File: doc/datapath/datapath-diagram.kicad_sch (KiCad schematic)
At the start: 24 parts, among them U17 ip, U19 insn, U27 stack[0], U28 stack[1], U29 ……, U32 cd_timer, U4 cstack[0], U5 cstack[1], U6 ……

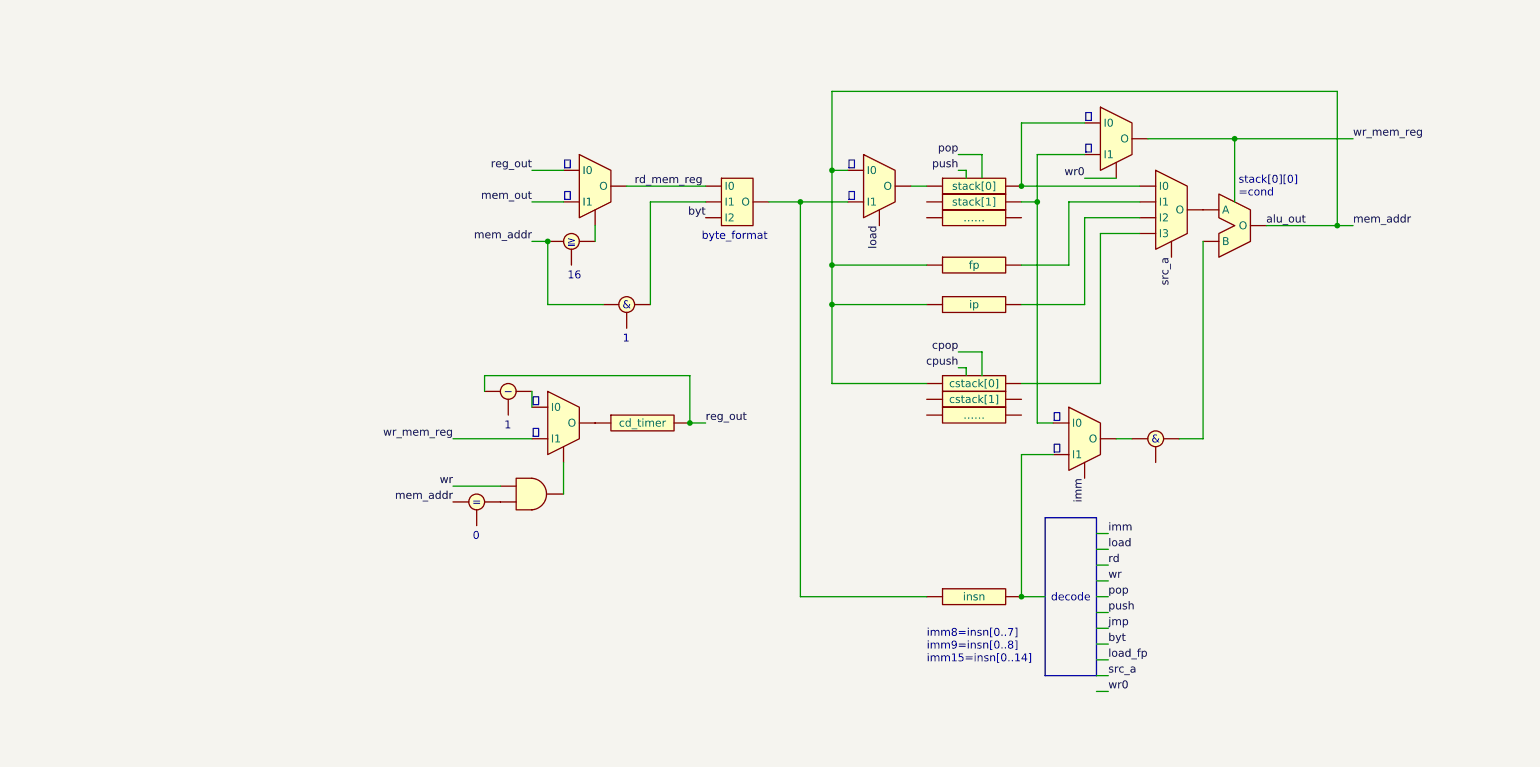
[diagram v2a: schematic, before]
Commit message: データパス図の信号名を現行の名前に合わせる
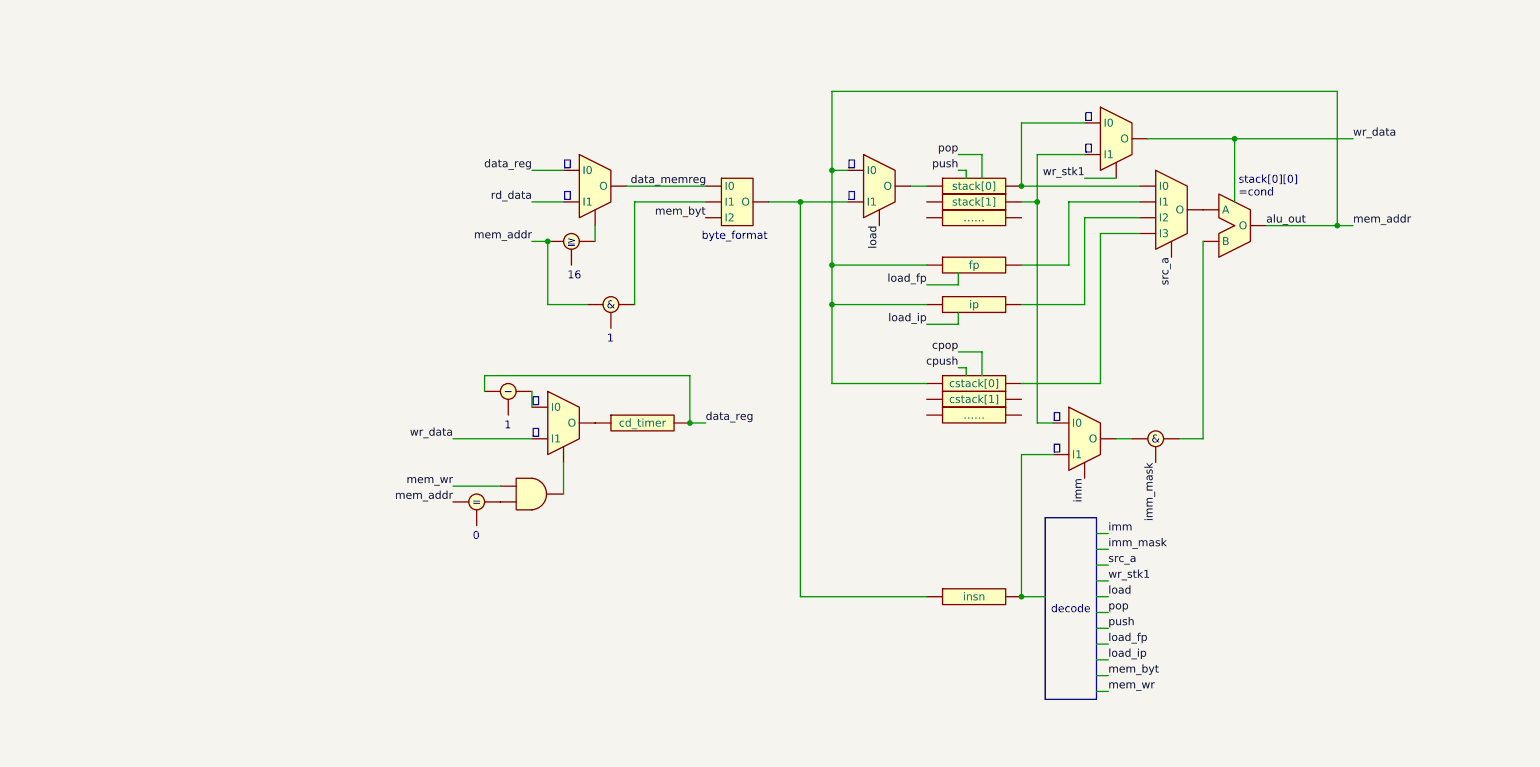
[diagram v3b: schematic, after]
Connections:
- net byt is gone; now on net mem_byt: U34. (O)
- net mem_out is gone; now on net rd_data: U31. (O)
- net wr is gone; now on net mem_wr: U39.
- net at U28.: now also U15. (O), U3. (O)
- net rd_data: now reaches U31. (O)
- net rd_data: no longer U1.
- net at U27.: now also U3. (O), U40. (O); no longer U18. (O)
- net data_reg: now reaches U32.
- net data_reg: now also U31. (O), U37.; no longer U36. (O)
- net mem_byt: now reaches U34. (O)
- net mem_byt: no longer U33.
- net wr_data: now reaches U36. (O)
- net wr_data: now also U3. (O); no longer U37.
- net imm_mask: now reaches U2.
- net mem_wr: now reaches U39.
- net mem_wr: no longer U36. (O)
- removed net rd_mem_reg: U31. (O), U34. (O)
- removed net reg_out: U31. (O), U32., U37.
- net wr0 renamed wr_stk1
- removed net wr_mem_reg: U3. (O), U36. (O)
- new net: U1., U31. (O)
- new net: U18. (O), U19., U34. (O)
- new net: U18. (O), U27.
- new net: U32., U36. (O)
- new net: U33., U34. (O)
- new net: U., U40. (O)
- new net: U17., U40. (O)
- new net: U4., U40. (O)
- new net: U12. (O), U40. (O)
- new net: U36. (O), U37.
- new net: U12. (O), U2.
- new net: U15. (O), U2.
- new net: U36. (O), U39.
- new net: U38., U39.
- new net data_memreg: U31. (O), U34. (O)
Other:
- note removed: "imm8=insn[0..7] imm9=insn[0..8] imm15=insn[0..14]"
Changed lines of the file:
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@@
     (stroke (width 0) (type default))
   )
-  (wire (pts (xy 114.3 69.85) (xy 114.3 53.34))
+  (wire (pts (xy 163.83 64.77) (xy 163.83 66.675))
+    (stroke (width 0) (type default))
+  )
+  (wire (pts (xy 111.76 69.85) (xy 111.76 53.34))
     (stroke (width 0) (type default))
   )
@@
     (stroke (width 0) (type default))
   )
-  (wire (pts (xy 97.79 69.85) (xy 106.68 69.85))
+  (wire (pts (xy 97.79 69.85) (xy 104.14 69.85))
     (stroke (width 0) (type default))
   )
@@
     (stroke (width 0) (type default))
   )
+  (wire (pts (xy 158.75 73.025) (xy 163.83 73.025))
+    (stroke (width 0) (type default))
+  )
   (wire (pts (xy 184.15 49.53) (xy 189.23 49.53))
     (stroke (width 0) (type default))
@@
     (stroke (width 0) (type default))
   )
+  (wire (pts (xy 110.49 50.8) (xy 123.19 50.8))
+    (stroke (width 0) (type default))
+  )
   (wire (pts (xy 97.79 59.69) (xy 97.79 69.85))
     (stroke (width 0) (type default))
@@
     (stroke (width 0) (type default))
   )
-  (wire (pts (xy 110.49 50.8) (xy 123.19 50.8))
+  (wire (pts (xy 163.83 71.12) (xy 163.83 73.025))
     (stroke (width 0) (type default))
   )
@@
     (stroke (width 0) (type default))
   )
+  (wire (pts (xy 158.75 66.675) (xy 163.83 66.675))
+    (stroke (width 0) (type default))
+  )
   (wire (pts (xy 208.28 43.18) (xy 208.28 53.34))
     (stroke (width 0) (type default))
@@
     (stroke (width 0) (type default))
   )
-  (wire (pts (xy 114.3 53.34) (xy 123.19 53.34))
+  (wire (pts (xy 111.76 53.34) (xy 123.19 53.34))
     (stroke (width 0) (type default))
   )
@@
   )
   (text_box "decode"
-    (at 177.8 104.14 0) (size 8.255 25.4)
+    (at 177.8 104.14 0) (size 8.255 29.21)
     (stroke (width 0) (type default))
     (fill (type color) (color 255 255 194 1))
@@
   )
   (text_box "&"
-    (at 109.22 68.58 0) (size 2.54 2.54)
+    (at 106.68 68.58 0) (size 2.54 2.54)
     (stroke (width -0.0001) (type default))
     (fill (type none))
@@
     (effects (font (size 1.27 1.27)) (justify left bottom))
   )
-  (text "imm8=insn[0..7]\nimm9=insn[0..8]\nimm15=insn[0..14]" (at 158.75 127.635 0)
-    (effects (font (size 1.27 1.27)) (justify left bottom))
-  )
   (text "偽" (at 146.05 48.26 0)
     (effects (font (size 1.27 1.27)) (justify left bottom))
@@
     (effects (font (size 1.27 1.27)) (justify left bottom))
   )
-  (text "1" (at 109.855 76.2 0)
+  (text "1" (at 107.315 76.2 0)
     (effects (font (size 1.27 1.27)) (justify left bottom))
   )
@@
     (effects (font (size 1.27 1.27)) (justify left bottom))
   )
-  (label "src_a" (at 187.96 129.54 0) (fields_autoplaced)
-    (effects (font (size 1.27 1.27)) (justify left bottom))
-  )
-  (label "mem_out" (at 95.25 53.34 180) (fields_autoplaced)
+  (label "src_a" (at 187.96 111.76 0) (fields_autoplaced)
+    (effects (font (size 1.27 1.27)) (justify left bottom))
+  )
+  (label "rd_data" (at 95.25 53.34 180) (fields_autoplaced)
     (effects (font (size 1.27 1.27)) (justify right bottom))
   )
@@
     (effects (font (size 1.27 1.27)) (justify right bottom))
   )
-  (label "wr_mem_reg" (at 227.33 43.18 0) (fields_autoplaced)
+  (label "imm_mask" (at 195.58 95.25 270) (fields_autoplaced)
+    (effects (font (size 1.27 1.27)) (justify right bottom))
+  )
+  (label "wr_data" (at 227.33 43.18 0) (fields_autoplaced)
     (effects (font (size 1.27 1.27)) (justify left bottom))
   )
@@
     (effects (font (size 1.27 1.27)) (justify right bottom))
   )
-  (label "wr" (at 187.96 114.3 0) (fields_autoplaced)
+  (label "imm_mask" (at 187.96 109.22 0) (fields_autoplaced)
+    (effects (font (size 1.27 1.27)) (justify left bottom))
+  )
+  (label "mem_wr" (at 187.96 132.08 0) (fields_autoplaced)
     (effects (font (size 1.27 1.27)) (justify left bottom))
   )
@@
     (effects (font (size 1.27 1.27)) (justify right bottom))
   )
-  (label "byt" (at 187.96 124.46 0) (fields_autoplaced)
+  (label "load_fp" (at 158.75 66.675 180) (fields_autoplaced)
+    (effects (font (size 1.27 1.27)) (justify right bottom))
+  )
+  (label "mem_byt" (at 187.96 129.54 0) (fields_autoplaced)
     (effects (font (size 1.27 1.27)) (justify left bottom))
   )
@@
     (effects (font (size 1.27 1.27)) (justify right bottom))
   )
-  (label "wr" (at 82.55 99.06 180) (fields_autoplaced)
+  (label "mem_wr" (at 82.55 99.06 180) (fields_autoplaced)
     (effects (font (size 1.27 1.27)) (justify right bottom))
   )
@@
     (effects (font (size 1.27 1.27)) (justify left bottom))
   )
-  (label "wr_mem_reg" (at 82.55 91.44 180) (fields_autoplaced)
+  (label "wr_data" (at 82.55 91.44 180) (fields_autoplaced)
     (effects (font (size 1.27 1.27)) (justify right bottom))
   )
@@
     (effects (font (size 1.27 1.27)) (justify left bottom))
   )
-  (label "reg_out" (at 95.25 48.26 180) (fields_autoplaced)
-    (effects (font (size 1.27 1.27)) (justify right bottom))
-  )
-  (label "push" (at 187.96 119.38 0) (fields_autoplaced)
+  (label "data_reg" (at 95.25 48.26 180) (fields_autoplaced)
+    (effects (font (size 1.27 1.27)) (justify right bottom))
+  )
+  (label "push" (at 187.96 121.92 0) (fields_autoplaced)
     (effects (font (size 1.27 1.27)) (justify left bottom))
   )
@@
     (effects (font (size 1.27 1.27)) (justify left bottom))
   )
-  (label "rd" (at 187.96 111.76 0) (fields_autoplaced)
-    (effects (font (size 1.27 1.27)) (justify left bottom))
-  )
-  (label "jmp" (at 187.96 121.92 0) (fields_autoplaced)
+  (label "load_ip" (at 187.96 127 0) (fields_autoplaced)
     (effects (font (size 1.27 1.27)) (justify left bottom))
   )
@@
     (effects (font (size 1.27 1.27)) (justify right bottom))
   )
-  (label "wr0" (at 184.15 49.53 180) (fields_autoplaced)
-    (effects (font (size 1.27 1.27)) (justify right bottom))
-  )
-  (label "wr0" (at 187.96 132.08 0) (fields_autoplaced)
-    (effects (font (size 1.27 1.27)) (justify left bottom))
-  )
-  (label "pop" (at 187.96 116.84 0) (fields_autoplaced)
-    (effects (font (size 1.27 1.27)) (justify left bottom))
-  )
-  (label "reg_out" (at 123.19 88.9 0) (fields_autoplaced)
-    (effects (font (size 1.27 1.27)) (justify left bottom))
-  )
-  (label "load_fp" (at 187.96 127 0) (fields_autoplaced)
-    (effects (font (size 1.27 1.27)) (justify left bottom))
-  )
-  (label "rd_mem_reg" (at 111.76 50.8 0) (fields_autoplaced)
-    (effects (font (size 1.27 1.27)) (justify left bottom))
-  )
-  (label "byt" (at 123.19 55.88 180) (fields_autoplaced)
-    (effects (font (size 1.27 1.27)) (justify right bottom))
-  )
-  (label "load" (at 187.96 109.22 0) (fields_autoplaced)
+  (label "wr_stk1" (at 184.15 49.53 180) (fields_autoplaced)
+    (effects (font (size 1.27 1.27)) (justify right bottom))
+  )
+  (label "wr_stk1" (at 187.96 114.3 0) (fields_autoplaced)
+    (effects (font (size 1.27 1.27)) (justify left bottom))
+  )
+  (label "pop" (at 187.96 119.38 0) (fields_autoplaced)
+    (effects (font (size 1.27 1.27)) (justify left bottom))
+  )
+  (label "data_reg" (at 123.19 88.9 0) (fields_autoplaced)
+    (effects (font (size 1.27 1.27)) (justify left bottom))
+  )
+  (label "load_fp" (at 187.96 124.46 0) (fields_autoplaced)
+    (effects (font (size 1.27 1.27)) (justify left bottom))
+  )
+  (label "data_memreg" (at 111.125 50.8 0) (fields_autoplaced)
+    (effects (font (size 1.27 1.27)) (justify left bottom))
+  )
+  (label "load_ip" (at 158.75 73.025 180) (fields_autoplaced)
+    (effects (font (size 1.27 1.27)) (justify right bottom))
+  )
+  (label "mem_byt" (at 123.19 55.88 180) (fields_autoplaced)
+    (effects (font (size 1.27 1.27)) (justify right bottom))
+  )
+  (label "load" (at 187.96 116.84 0) (fields_autoplaced)
     (effects (font (size 1.27 1.27)) (justify left bottom))
   )
@@
     )
   )
-  (symbol (lib_id "Logic_Component:ALU_Circle_Left_Bottom") (at 110.49 69.85 0) (unit 1)
+  (symbol (lib_id "Logic_Component:ALU_Circle_Left_Bottom") (at 107.95 69.85 0) (unit 1)
     (in_bom yes) (on_board yes) (dnp no) (fields_autoplaced)
-    (property "Reference" "U33" (at 110.49 67.31 0)
-      (effects (font (size 1.27 1.27)) hide)
-    )
-    (property "Value" "~" (at 110.49 69.85 0)
+    (property "Reference" "U33" (at 107.95 67.31 0)
+      (effects (font (size 1.27 1.27)) hide)
+    )
+    (property "Value" "~" (at 107.95 69.85 0)
       (effects (font (size 1.27 1.27)))
     )
-    (property "Footprint" "" (at 110.49 69.85 0)
-      (effects (font (size 1.27 1.27)) hide)
-    )
-    (property "Datasheet" "" (at 110.49 69.85 0)
-      (effects (font (size 1.27 1.27)) hide)
-    )
+    (property "Footprint" "" (at 107.95 69.85 0)
+      (effects (font (size 1.27 1.27)) hide)
+    )
+    (property "Datasheet" "" (at 107.95 69.85 0)
+      (effects (font (size 1.27 1.27)) hide)
+    )

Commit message: デコーダに cpop と cpush を追加
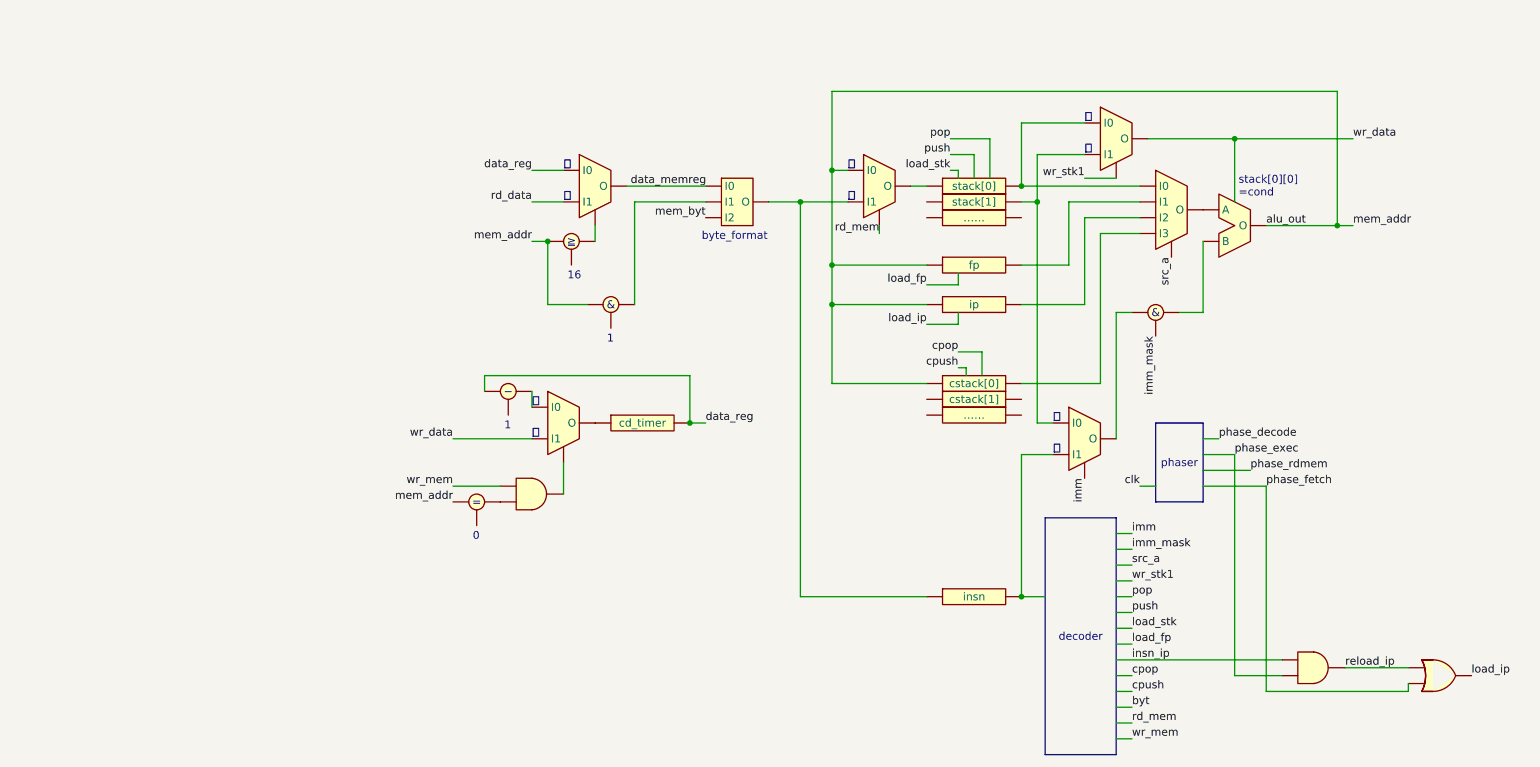
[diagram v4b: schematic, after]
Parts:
- added U7: ~, symbol Logic_Component:Gate_AND_2Input
- added U8: ~, symbol Logic_Component:Gate_OR_2Input
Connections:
- net mem_wr is gone; now on net wr_mem: U39.
- net load_ip: now also U8.
- net at U28.: now also U15. (O), U3. (O)
- net at U27.: now also U3. (O), U40. (O); no longer U18. (O)
- net wr_mem: now reaches U39.
- net wr_mem: no longer U36. (O)
- net load renamed rd_mem
- new net: U1., U31. (O)
- new net: U18. (O), U19., U34. (O)
- new net: U18. (O), U27.
- new net: U32., U36. (O)
- new net: U33., U34. (O)
- new net: U., U40. (O)
- new net: U17., U40. (O)
- new net: U4., U40. (O)
- new net: U12. (O), U40. (O)
- new net: U36. (O), U37.
- new net: U12. (O), U2.
- new net: U15. (O), U2.
- new net: U36. (O), U39.
- new net: U38., U39.
- new net insn_ip: U7.
- new net phase_exec: U7.
- new net phase_fetch: U8.
- new net reload_ip: U7., U8.
